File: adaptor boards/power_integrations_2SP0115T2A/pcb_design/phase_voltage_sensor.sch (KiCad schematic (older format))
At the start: 10 parts, among them U3 AMC1301

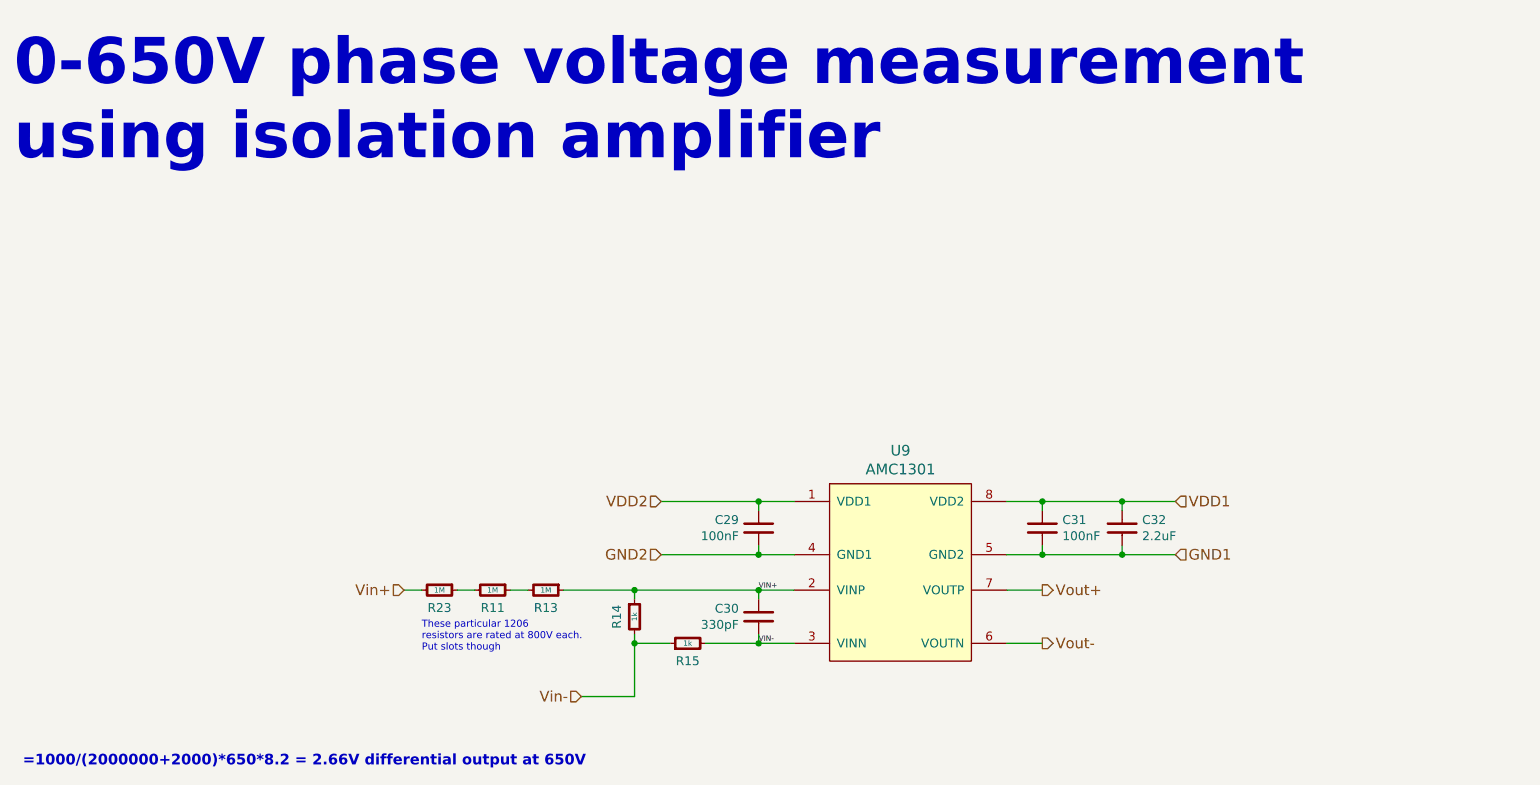
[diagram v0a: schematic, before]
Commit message: Fix swapped differential signals in the interface board
Signed-off-by: Marcos Chaparro <mchaparro@paltatech.com>
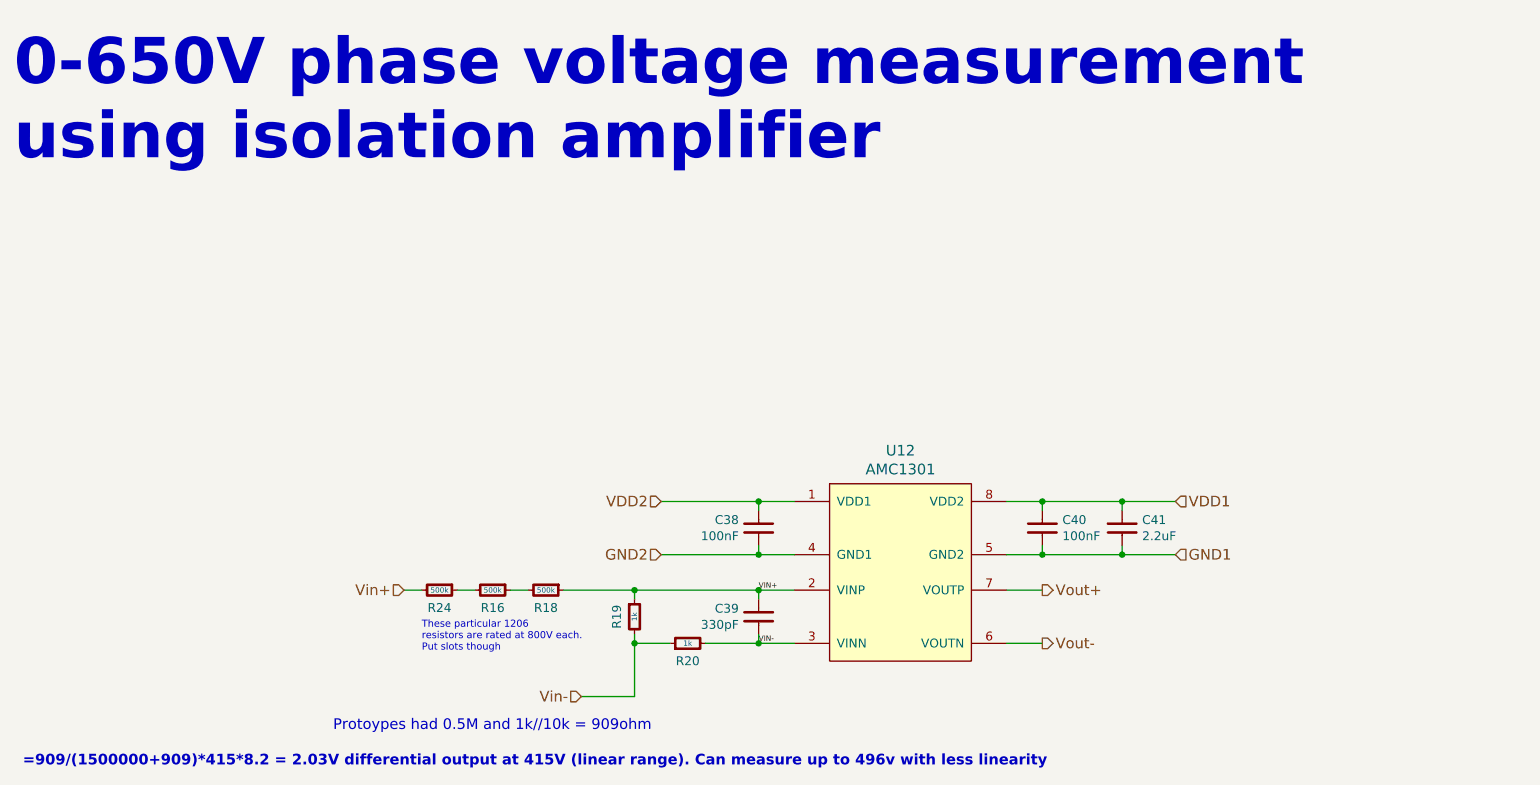
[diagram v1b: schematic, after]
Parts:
- C20, C22: MFR (none) -> Murata Electronics North America; MPN (none) -> GRM188R71E104KA01D; SPN (none) -> 490-1524-1-ND; SPR (none) -> Digikey
- C21: MFR (none) -> Murata Electronics North America; MPN (none) -> GCM1885C1H331JA16D; SPN (none) -> 490-4964-1-ND; SPR (none) -> Digikey
- C23: MFR (none) -> Murata Electronics North America; MPN (none) -> GRM188R71A225KE15D; SPN (none) -> 490-4520-1-ND; SPR (none) -> Digikey
- R10, R9: MFR (none) -> Yageo; MPN (none) -> RC0603FR-071KL; SPN (none) -> 311-1.00KHRCT-ND; SPR (none) -> Digikey
- R22, R6, R8: value 1M -> 500k; MFR (none) -> Yageo; MPN (none) -> AC1206FR-071ML; SPN (none) -> YAG3832CT-ND; SPR (none) -> Digikey
- U3: #mfg AMC1301DWVR -> (none); MFR (none) -> Texas Instruments; MPN (none) -> AMC1301DWVR; SPN (none) -> 296-44577-1-ND; SPR (none) -> Digikey
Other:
- note added: "=909/(1500000+909)*415*8.2 = 2.03V differential output at 415V (linear range). Can measure up to 496v with less linearity"
- note added: "Protoypes had 0.5M and 1k//10k = 909ohm"
- note removed: "=1000/(2000000+2000)*650*8.2 = 2.66V differential output at 650V"
